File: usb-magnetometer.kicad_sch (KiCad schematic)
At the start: 43 parts, among them J1 USB_C_Receptacle_USB2.0, J2 1x5_MALE, J3 1x2_Male, U1 FT231XS, U2 TMAG5170, U3 STM32L010C6T6

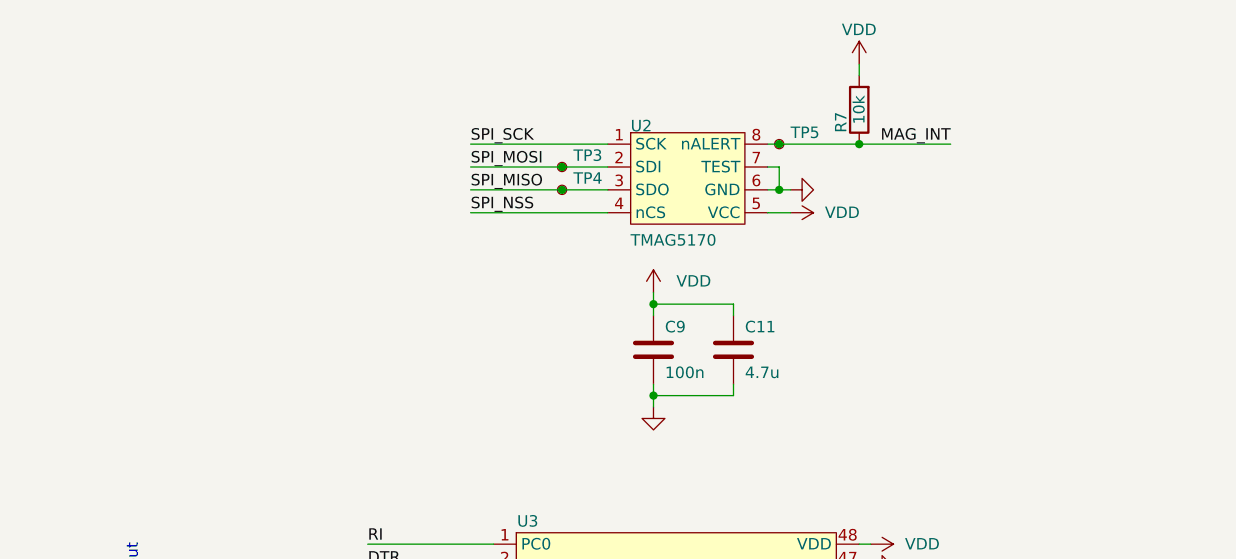
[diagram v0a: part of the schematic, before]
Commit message: Add initial version of separated pcbs
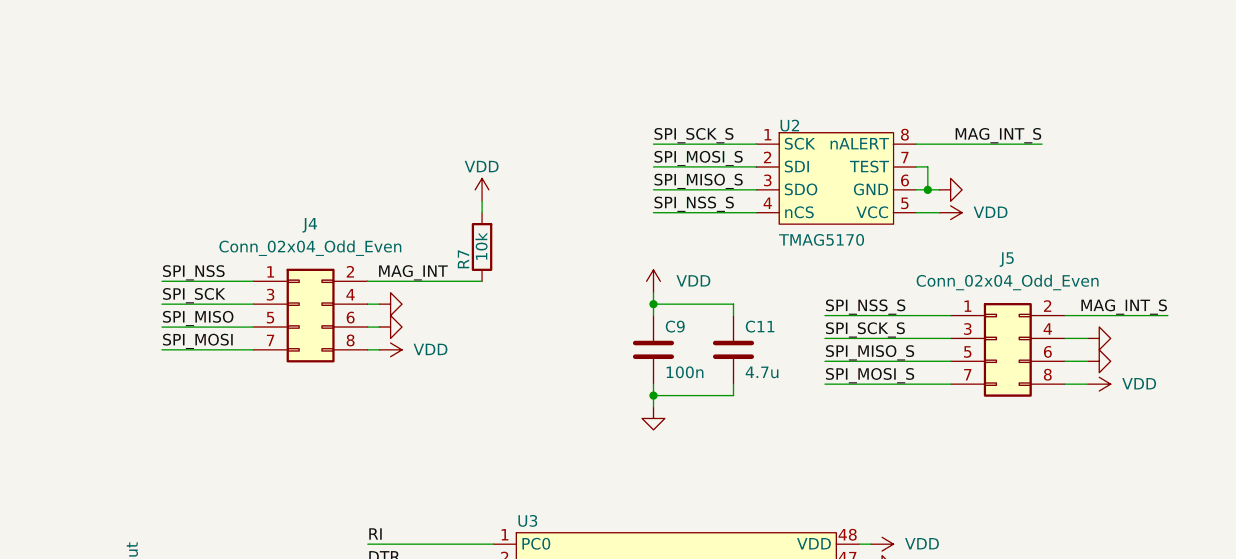
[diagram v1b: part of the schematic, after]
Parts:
- removed TP3, TP4, TP5: TestPoint_Small, TestPoint:TestPoint_Pad_D1.0mm, symbol Connector:TestPoint_Small
- added J4: Conn_02x04_Odd_Even, Connector_PinSocket_1.27mm:PinSocket_2x04_P1.27mm_Horizontal, symbol Connector_Generic:Conn_02x04_Odd_Even
- added J5: Conn_02x04_Odd_Even, Connector_PinHeader_1.27mm:PinHeader_2x04_P1.27mm_Horizontal, symbol Connector_Generic:Conn_02x04_Odd_Even
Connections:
- net GND: now also J4.4 (Pin_4), J4.6 (Pin_6), J5.4 (Pin_4), J5.6 (Pin_6)
- net MAG_INT: now also J4.2 (Pin_2); no longer U2.8 (nALERT)
- net SPI_MISO: now also J4.5 (Pin_5); no longer U2.3 (SDO)
- net SPI_MOSI: now also J4.7 (Pin_7); no longer U2.2 (SDI)
- net SPI_NSS: now also J4.1 (Pin_1); no longer U2.4 (nCS)
- net SPI_SCK: now also J4.3 (Pin_3); no longer U2.1 (SCK)
- net VDD: now also J4.8 (Pin_8), J5.8 (Pin_8)
- new net MAG_INT_S: J5.2 (Pin_2), U2.8 (nALERT)
- new net SPI_MISO_S: J5.5 (Pin_5), U2.3 (SDO)
- new net SPI_MOSI_S: J5.7 (Pin_7), U2.2 (SDI)
- new net SPI_NSS_S: J5.1 (Pin_1), U2.4 (nCS)
- new net SPI_SCK_S: J5.3 (Pin_3), U2.1 (SCK)
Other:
- moved on the sheet: R7, U2

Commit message: FPC connectors in progress
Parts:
- added J6, J7: Conn_02x04_Odd_Even, Connector_PinHeader_1.00mm:PinHeader_2x04_P1.00mm_Vertical, symbol Connector_Generic:Conn_02x04_Odd_Even
- J4: footprint Connector_PinSocket_1.27mm:PinSocket_2x04_P1.27mm_Horizontal -> Connector_FFC-FPC:Hirose_FH12-8S-0.5SH_1x08-1MP_P0.50mm_Horizontal
- J5: footprint Connector_PinHeader_1.27mm:PinHeader_2x04_P1.27mm_Horizontal -> Connector_FFC-FPC:Hirose_FH12-8S-0.5SH_1x08-1MP_P0.50mm_Horizontal
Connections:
- net GND: now also J5.2 (Pin_2), J5.5 (Pin_5), J7.4 (Pin_4), J7.6 (Pin_6); no longer C11.2, C9.2, J4.4 (Pin_4), J4.6 (Pin_6), J5.4 (Pin_4), J5.6 (Pin_6), U2.6 (GND), U2.7 (TEST)
- net MAG_INT: now also J5.8 (Pin_8), J7.2 (Pin_2); no longer J4.2 (Pin_2)
- net MAG_INT_S: now also J4.1 (Pin_1), J6.8 (Pin_8); no longer J5.2 (Pin_2)
- net SPI_MISO: now also J5.4 (Pin_4), J7.5 (Pin_5); no longer J4.5 (Pin_5)
- net SPI_MISO_S: now also J4.5 (Pin_5), J6.2 (Pin_2); no longer J5.5 (Pin_5)
- net SPI_MOSI: now also J5.3 (Pin_3), J7.7 (Pin_7); no longer J4.7 (Pin_7)
- net SPI_MOSI_S: now also J4.6 (Pin_6), J6.4 (Pin_4); no longer J5.7 (Pin_7)
- net SPI_NSS: now also J5.6 (Pin_6), J7.1 (Pin_1); no longer J4.1 (Pin_1)
- net SPI_NSS_S: now also J4.3 (Pin_3), J6.1 (Pin_1); no longer J5.1 (Pin_1)
- net SPI_SCK: now also J5.1 (Pin_1), J7.3 (Pin_3); no longer J4.3 (Pin_3)
- net SPI_SCK_S: now also J4.8 (Pin_8), J6.6 (Pin_6); no longer J5.3 (Pin_3)
- net VDD: now also J5.7 (Pin_7), J7.8 (Pin_8); no longer C11.1, C9.1, J4.8 (Pin_8), J5.8 (Pin_8), U2.5 (VCC)
- new net GND_S: C11.2, C9.2, J4.4 (Pin_4), J4.7 (Pin_7), J6.3 (Pin_3), J6.5 (Pin_5), U2.6 (GND), U2.7 (TEST)
- new net VDD_S: C11.1, C9.1, J4.2 (Pin_2), J6.7 (Pin_7), U2.5 (VCC)
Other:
- moved on the sheet: C11, C9, J3, J4, J5, R7

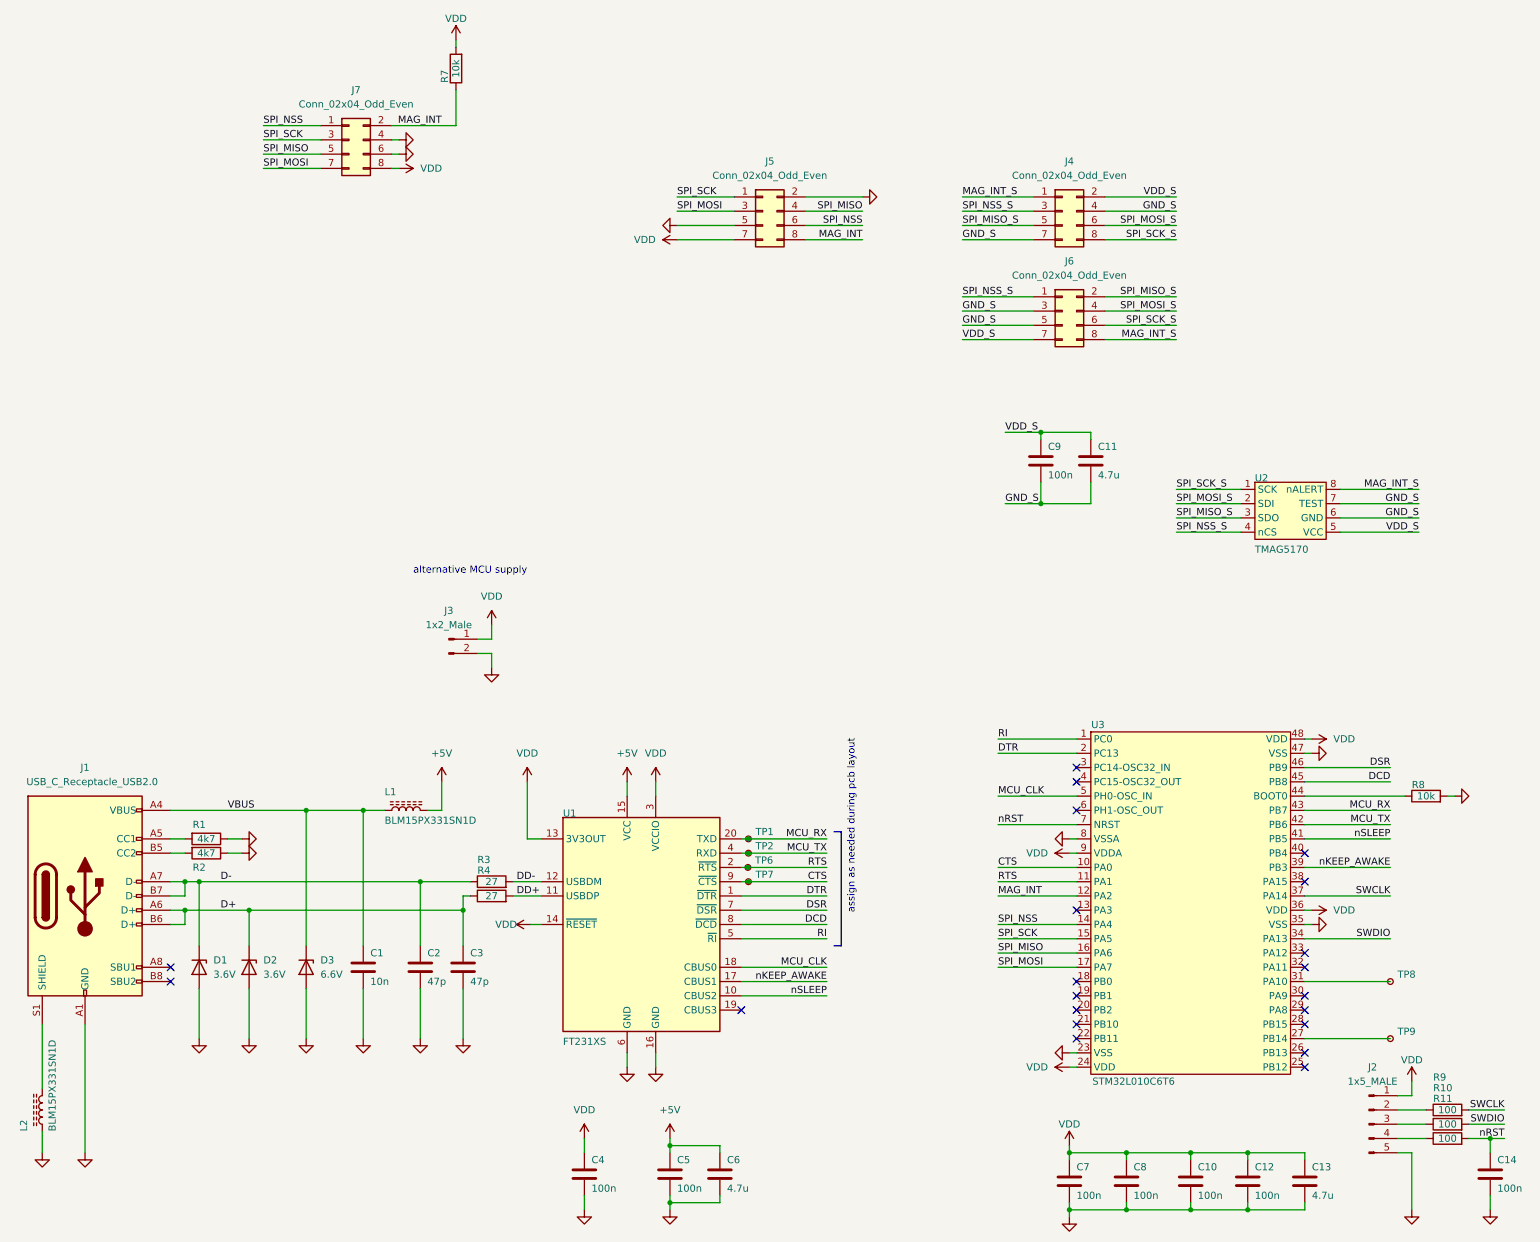
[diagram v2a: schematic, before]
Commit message: Add final version with sensor on separated pcb
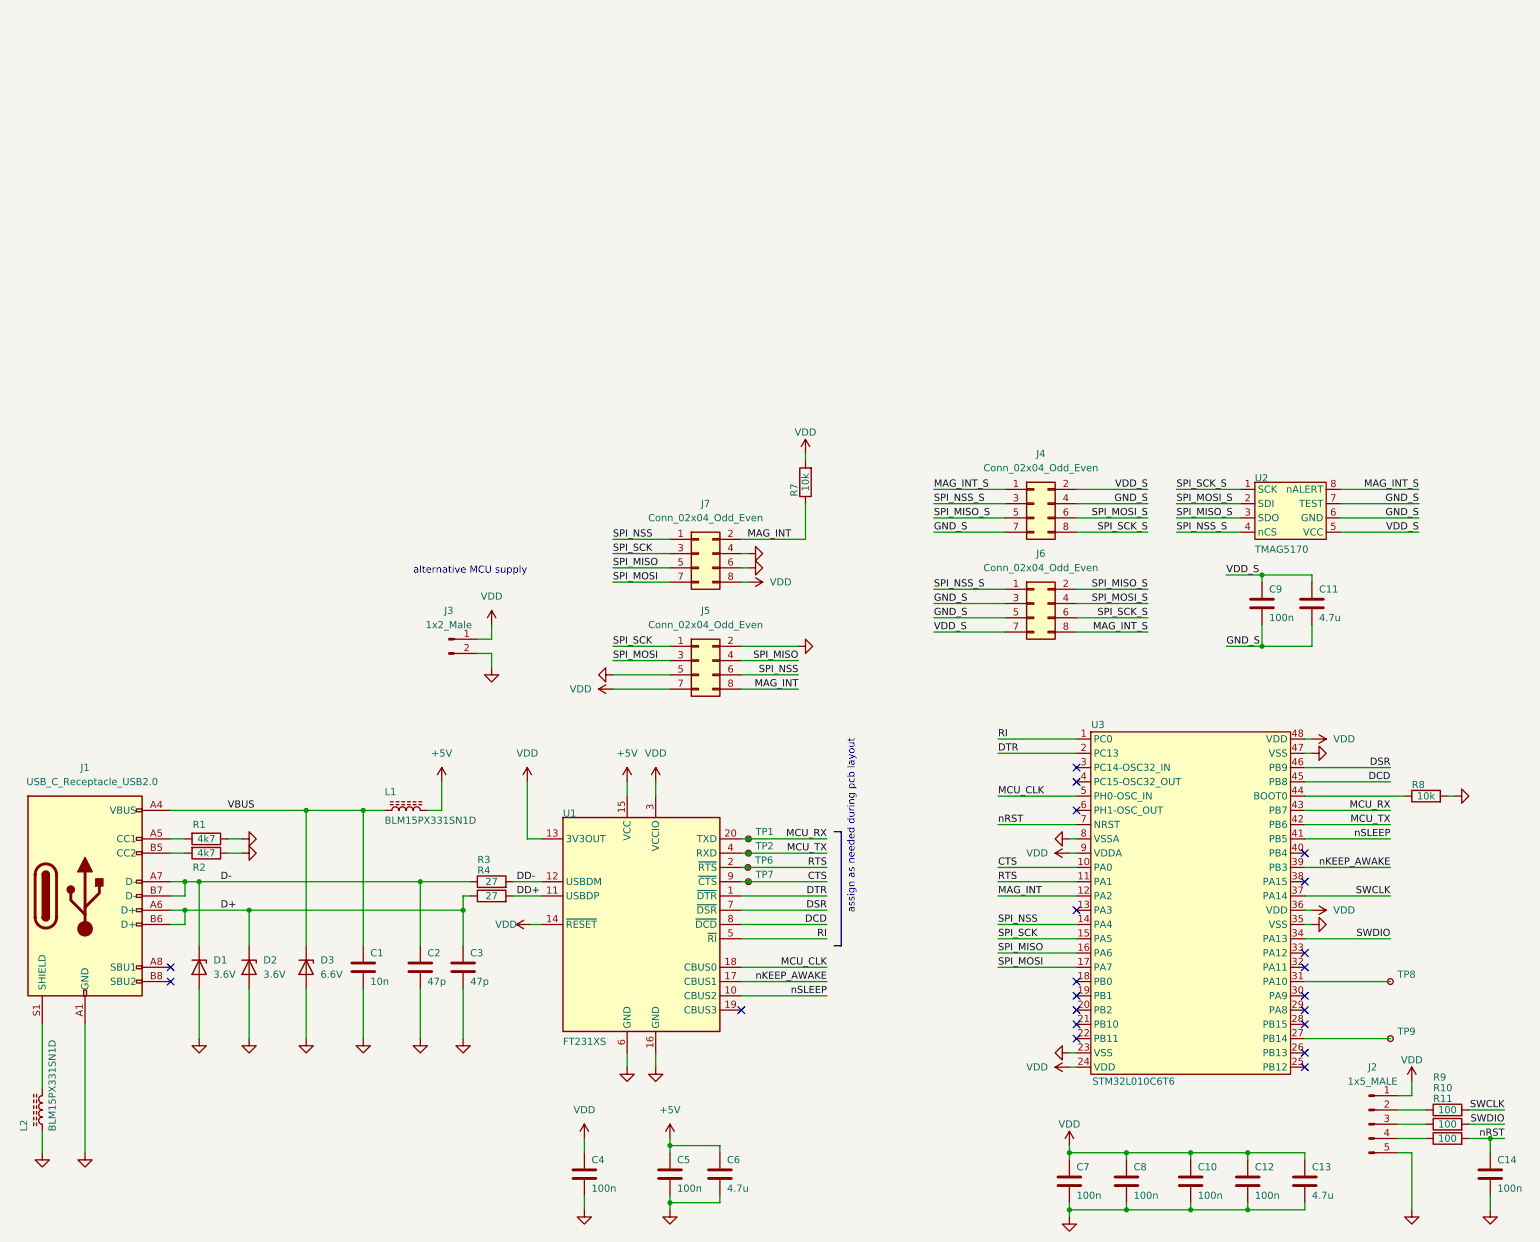
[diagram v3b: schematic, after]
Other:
- moved on the sheet: C11, C9, J4, J5, J6, J7, R7
